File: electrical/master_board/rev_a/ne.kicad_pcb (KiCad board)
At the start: 2 copper layers, 0 parts

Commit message: Inject the PCB outlines into master/center/ne/nw/se/sw PCB's.
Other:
- board outline added: 42.2 x 39 mm
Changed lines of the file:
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@@
     (uvia_drill 0.1)
   )
+  (gr_line (start 162.50 64.00) (end 170.67 64.00) (layer Edge.Cuts) (width 0.05))
+  (gr_line (start 170.67 64.00) (end 170.80 63.99) (layer Edge.Cuts) (width 0.05))
+  (gr_line (start 170.80 63.99) (end 170.93 63.98) (layer Edge.Cuts) (width 0.05))
+  (gr_line (start 170.93 63.98) (end 171.06 63.95) (layer Edge.Cuts) (width 0.05))
+  (gr_line (start 171.06 63.95) (end 171.19 63.90) (layer Edge.Cuts) (width 0.05))
+  (gr_line (start 171.19 63.90) (end 171.32 63.85) (layer Edge.Cuts) (width 0.05))
+  (gr_line (start 171.32 63.85) (end 171.43 63.79) (layer Edge.Cuts) (width 0.05))
+  (gr_line (start 171.43 63.79) (end 171.55 63.72) (layer Edge.Cuts) (width 0.05))
+  (gr_line (start 171.55 63.72) (end 171.65 63.63) (layer Edge.Cuts) (width 0.05))
+  (gr_line (start 171.65 63.63) (end 171.75 63.54) (layer Edge.Cuts) (width 0.05))
+  (gr_line (start 171.75 63.54) (end 171.84 63.44) (layer Edge.Cuts) (width 0.05))
+  (gr_line (start 171.84 63.44) (end 171.92 63.33) (layer Edge.Cuts) (width 0.05))
+  (gr_line (start 171.92 63.33) (end 171.99 63.21) (layer Edge.Cuts) (width 0.05))
+  (gr_line (start 171.99 63.21) (end 172.04 63.09) (layer Edge.Cuts) (width 0.05))
+  (gr_line (start 172.04 63.09) (end 172.09 62.97) (layer Edge.Cuts) (width 0.05))
+  (gr_line (start 172.09 62.97) (end 172.13 62.84) (layer Edge.Cuts) (width 0.05))
+  (gr_line (start 172.13 62.84) (end 172.15 62.71) (layer Edge.Cuts) (width 0.05))
+  (gr_line (start 172.15 62.71) (end 172.16 62.57) (layer Edge.Cuts) (width 0.05))
+  (gr_line (start 172.16 62.57) (end 172.17 62.44) (layer Edge.Cuts) (width 0.05))
+  (gr_line (start 172.17 62.44) (end 172.15 62.31) (layer Edge.Cuts) (width 0.05))
+  (gr_line (start 172.15 62.31) (end 172.13 62.17) (layer Edge.Cuts) (width 0.05))
+  (gr_line (start 172.13 62.17) (end 172.10 62.04) (layer Edge.Cuts) (width 0.05))
+  (gr_line (start 172.10 62.04) (end 172.05 61.92) (layer Edge.Cuts) (width 0.05))
+  (gr_line (start 172.05 61.92) (end 171.99 61.80) (layer Edge.Cuts) (width 0.05))
+  (gr_line (start 171.99 61.80) (end 171.99 61.80) (layer Edge.Cuts) (width 0.05))
+  (gr_line (start 171.99 61.80) (end 167.96 55.01) (layer Edge.Cuts) (width 0.05))
+  (gr_line (start 167.96 55.01) (end 163.29 48.65) (layer Edge.Cuts) (width 0.05))
+  (gr_line (start 163.29 48.65) (end 158.02 42.77) (layer Edge.Cuts) (width 0.05))
+  (gr_line (start 158.02 42.77) (end 152.21 37.42) (layer Edge.Cuts) (width 0.05))
+  (gr_line (start 152.21 37.42) (end 145.92 32.67) (layer Edge.Cuts) (width 0.05))
+  (gr_line (start 145.92 32.67) (end 139.19 28.54) (layer Edge.Cuts) (width 0.05))
+  (gr_line (start 139.19 28.54) (end 132.09 25.08) (layer Edge.Cuts) (width 0.05))
+  (gr_line (start 132.09 25.08) (end 131.96 25.04) (layer Edge.Cuts) (width 0.05))
+  (gr_line (start 131.96 25.04) (end 131.83 25.00) (layer Edge.Cuts) (width 0.05))
+  (gr_line (start 131.83 25.00) (end 131.70 24.98) (layer Edge.Cuts) (width 0.05))
+  (gr_line (start 131.70 24.98) (end 131.57 24.96) (layer Edge.Cuts) (width 0.05))
+  (gr_line (start 131.57 24.96) (end 131.43 24.96) (layer Edge.Cuts) (width 0.05))
+  (gr_line (start 131.43 24.96) (end 131.30 24.98) (layer Edge.Cuts) (width 0.05))
+  (gr_line (start 131.30 24.98) (end 131.17 25.00) (layer Edge.Cuts) (width 0.05))
+  (gr_line (start 131.17 25.00) (end 131.04 25.04) (layer Edge.Cuts) (width 0.05))
+  (gr_line (start 131.04 25.04) (end 130.91 25.08) (layer Edge.Cuts) (width 0.05))
+  (gr_line (start 130.91 25.08) (end 130.79 25.14) (layer Edge.Cuts) (width 0.05))
+  (gr_line (start 130.79 25.14) (end 130.67 25.21) (layer Edge.Cuts) (width 0.05))
+  (gr_line (start 130.67 25.21) (end 130.57 25.29) (layer Edge.Cuts) (width 0.05))
+  (gr_line (start 130.57 25.29) (end 130.46 25.38) (layer Edge.Cuts) (width 0.05))
+  (gr_line (start 130.46 25.38) (end 130.37 25.48) (layer Edge.Cuts) (width 0.05))
+  (gr_line (start 130.37 25.48) (end 130.29 25.58) (layer Edge.Cuts) (width 0.05))
+  (gr_line (start 130.29 25.58) (end 130.21 25.69) (layer Edge.Cuts) (width 0.05))
+  (gr_line (start 130.21 25.69) (end 130.15 25.81) (layer Edge.Cuts) (width 0.05))
+  (gr_line (start 130.15 25.81) (end 130.10 25.94) (layer Edge.Cuts) (width 0.05))
+  (gr_line (start 130.10 25.94) (end 130.05 26.06) (layer Edge.Cuts) (width 0.05))
+  (gr_line (start 130.05 26.06) (end 130.02 26.19) (layer Edge.Cuts) (width 0.05))
+  (gr_line (start 130.02 26.19) (end 130.01 26.33) (layer Edge.Cuts) (width 0.05))
+  (gr_line (start 130.01 26.33) (end 130.00 26.46) (layer Edge.Cuts) (width 0.05))
+  (gr_line (start 130.00 26.46) (end 130.00 61.00) (layer Edge.Cuts) (width 0.05))
+  (gr_line (start 130.00 61.00) (end 161.00 61.00) (layer Edge.Cuts) (width 0.05))
+  (gr_line (start 161.00 61.00) (end 161.13 61.01) (layer Edge.Cuts) (width 0.05))
+  (gr_line (start 161.13 61.01) (end 161.26 61.02) (layer Edge.Cuts) (width 0.05))
+  (gr_line (start 161.26 61.02) (end 161.39 61.05) (layer Edge.Cuts) (width 0.05))
+  (gr_line (start 161.39 61.05) (end 161.51 61.09) (layer Edge.Cuts) (width 0.05))
+  (gr_line (start 161.51 61.09) (end 161.63 61.14) (layer Edge.Cuts) (width 0.05))
+  (gr_line (start 161.63 61.14) (end 161.75 61.20) (layer Edge.Cuts) (width 0.05))
+  (gr_line (start 161.75 61.20) (end 161.86 61.27) (layer Edge.Cuts) (width 0.05))
+  (gr_line (start 161.86 61.27) (end 161.96 61.35) (layer Edge.Cuts) (width 0.05))
+  (gr_line (start 161.96 61.35) (end 162.06 61.44) (layer Edge.Cuts) (width 0.05))
+  (gr_line (start 162.06 61.44) (end 162.15 61.54) (layer Edge.Cuts) (width 0.05))
+  (gr_line (start 162.15 61.54) (end 162.23 61.64) (layer Edge.Cuts) (width 0.05))
+  (gr_line (start 162.23 61.64) (end 162.30 61.75) (layer Edge.Cuts) (width 0.05))
+  (gr_line (start 162.30 61.75) (end 162.36 61.87) (layer Edge.Cuts) (width 0.05))
+  (gr_line (start 162.36 61.87) (end 162.41 61.99) (layer Edge.Cuts) (width 0.05))
+  (gr_line (start 162.41 61.99) (end 162.45 62.11) (layer Edge.Cuts) (width 0.05))
+  (gr_line (start 162.45 62.11) (end 162.48 62.24) (layer Edge.Cuts) (width 0.05))
+  (gr_line (start 162.48 62.24) (end 162.49 62.37) (layer Edge.Cuts) (width 0.05))
+  (gr_line (start 162.49 62.37) (end 162.50 62.50) (layer Edge.Cuts) (width 0.05))
+  (gr_line (start 162.50 62.50) (end 162.50 64.00) (layer Edge.Cuts) (width 0.05))
 )

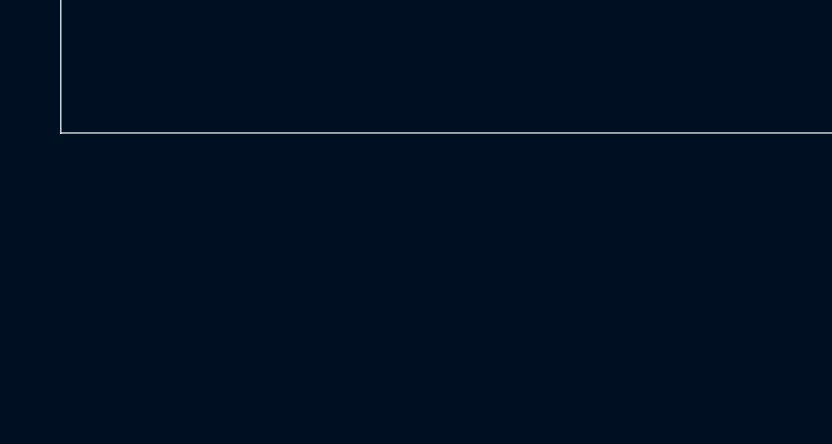
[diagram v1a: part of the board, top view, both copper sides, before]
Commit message: Have generated/footprint symbol in a KiCad project.
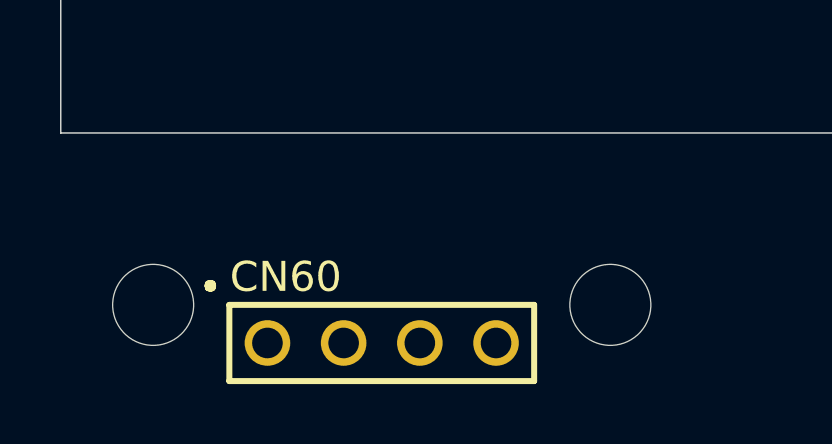
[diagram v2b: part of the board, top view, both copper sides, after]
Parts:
- added CN60: HCSR04H;F1X4, HR2:HCSR04_F1x4H_MATE, F.Cu at (140.7, 68.0)
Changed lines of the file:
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@@
   (general
     (thickness 1.6)
-    (drawings 0)
+    (drawings 75)
     (tracks 0)
     (zones 0)
-    (modules 0)
+    (modules 1)
     (nets 1)
   )
@@
     (47 F.CrtYd user)
     (48 B.Fab user)
-    (49 F.Fab user)
+    (49 F.Fab user hide)
   )
   (setup
@@
     (uvia_dia 0.3)
     (uvia_drill 0.1)
-  )
-  (gr_line (start 162.50 64.00) (end 170.67 64.00) (layer Edge.Cuts) (width 0.05))
-  (gr_line (start 170.67 64.00) (end 170.80 63.99) (layer Edge.Cuts) (width 0.05))
-  (gr_line (start 170.80 63.99) (end 170.93 63.98) (layer Edge.Cuts) (width 0.05))
+    (add_net "Net-(CN60-Pad1)")
+    (add_net "Net-(CN60-Pad2)")
+    (add_net "Net-(CN60-Pad3)")
+    (add_net "Net-(CN60-Pad4)")
+  )
+  (module HR2:HCSR04_F1x4H_MATE (layer F.Cu)
+    (at 140.7 68)
+    (fp_text reference CN60 (at -3.2 -2.2) (layer F.SilkS)
+      (effects (font (size 1 1) (thickness 0.2)))
+    )
+    (fp_text value HCSR04H;F1X4 (at 0 -2) (layer F.Fab)
+      (effects (font (size 1 1) (thickness 0.2)))
+    )
+    (fp_line (start 5.08 -1.27) (end 5.08 1.27) (layer F.SilkS) (width 0.2))
+    (fp_line (start 5.08 1.27) (end -5.08 1.27) (layer F.SilkS) (width 0.2))
+    (fp_line (start -5.08 1.27) (end -5.08 -1.27) (layer F.SilkS) (width 0.2))
+    (fp_line (start -5.08 -1.27) (end 5.08 -1.27) (layer F.SilkS) (width 0.2))
+    (fp_line (start -5.62 -1.91) (end -5.64 -1.98) (layer F.SilkS) (width 0.2))
+    (fp_line (start -5.64 -1.98) (end -5.71 -2) (layer F.SilkS) (width 0.2))
+    (fp_line (start -5.71 -2) (end -5.79 -1.98) (layer F.SilkS) (width 0.2))
+    (fp_line (start -5.79 -1.98) (end -5.81 -1.91) (layer F.SilkS) (width 0.2))
+    (fp_line (start -5.81 -1.91) (end -5.79 -1.83) (layer F.SilkS) (width 0.2))
+    (fp_line (start -5.79 -1.83) (end -5.71 -1.8) (layer F.SilkS) (width 0.2))
+    (fp_line (start -5.71 -1.8) (end -5.64 -1.83) (layer F.SilkS) (width 0.2))
+    (fp_line (start -5.64 -1.83) (end -5.62 -1.91) (layer F.SilkS) (width 0.2))
+    (pad "HCSR04 West Tie Down Hole" np_thru_hole circle (at -7.62 -1.27) (size 2.7 2.7) (drill 2.7) (layers *.Cu *.Mask))
+    (pad "HCSR04 East Tie Down Hole" np_thru_hole circle (at 7.62 -1.27) (size 2.7 2.7) (drill 2.7) (layers *.Cu *.Mask))
+    (pad 4 thru_hole circle (at 3.81 0) (size 1.52 1.52) (drill 1.02) (layers *.Cu *.Mask))
+    (pad 3 thru_hole circle (at 1.27 0) (size 1.52 1.52) (drill 1.02) (layers *.Cu *.Mask))
+    (pad 2 thru_hole circle (at -1.27 0) (size 1.52 1.52) (drill 1.02) (layers *.Cu *.Mask))
+    (pad 1 thru_hole circle (at -3.81 0) (size 1.52 1.52) (drill 1.02) (layers *.Cu *.Mask))
+  )
+  (gr_line (start 162.5 64) (end 170.67 64) (layer Edge.Cuts) (width 0.05))
+  (gr_line (start 170.67 64) (end 170.8 63.99) (layer Edge.Cuts) (width 0.05))
+  (gr_line (start 170.8 63.99) (end 170.93 63.98) (layer Edge.Cuts) (width 0.05))
   (gr_line (start 170.93 63.98) (end 171.06 63.95) (layer Edge.Cuts) (width 0.05))
-  (gr_line (start 171.06 63.95) (end 171.19 63.90) (layer Edge.Cuts) (width 0.05))
-  (gr_line (start 171.19 63.90) (end 171.32 63.85) (layer Edge.Cuts) (width 0.05))
+  (gr_line (start 171.06 63.95) (end 171.19 63.9) (layer Edge.Cuts) (width 0.05))
+  (gr_line (start 171.19 63.9) (end 171.32 63.85) (layer Edge.Cuts) (width 0.05))
   (gr_line (start 171.32 63.85) (end 171.43 63.79) (layer Edge.Cuts) (width 0.05))
   (gr_line (start 171.43 63.79) (end 171.55 63.72) (layer Edge.Cuts) (width 0.05))
@@
   (gr_line (start 172.17 62.44) (end 172.15 62.31) (layer Edge.Cuts) (width 0.05))
   (gr_line (start 172.15 62.31) (end 172.13 62.17) (layer Edge.Cuts) (width 0.05))
-  (gr_line (start 172.13 62.17) (end 172.10 62.04) (layer Edge.Cuts) (width 0.05))
-  (gr_line (start 172.10 62.04) (end 172.05 61.92) (layer Edge.Cuts) (width 0.05))
-  (gr_line (start 172.05 61.92) (end 171.99 61.80) (layer Edge.Cuts) (width 0.05))
-  (gr_line (start 171.99 61.80) (end 171.99 61.80) (layer Edge.Cuts) (width 0.05))
-  (gr_line (start 171.99 61.80) (end 167.96 55.01) (layer Edge.Cuts) (width 0.05))
+  (gr_line (start 172.13 62.17) (end 172.1 62.04) (layer Edge.Cuts) (width 0.05))
+  (gr_line (start 172.1 62.04) (end 172.05 61.92) (layer Edge.Cuts) (width 0.05))
+  (gr_line (start 172.05 61.92) (end 171.99 61.8) (layer Edge.Cuts) (width 0.05))
+  (gr_line (start 171.99 61.8) (end 171.99 61.8) (layer Edge.Cuts) (width 0.05))
+  (gr_line (start 171.99 61.8) (end 167.96 55.01) (layer Edge.Cuts) (width 0.05))
   (gr_line (start 167.96 55.01) (end 163.29 48.65) (layer Edge.Cuts) (width 0.05))
   (gr_line (start 163.29 48.65) (end 158.02 42.77) (layer Edge.Cuts) (width 0.05))
@@
   (gr_line (start 139.19 28.54) (end 132.09 25.08) (layer Edge.Cuts) (width 0.05))
   (gr_line (start 132.09 25.08) (end 131.96 25.04) (layer Edge.Cuts) (width 0.05))
-  (gr_line (start 131.96 25.04) (end 131.83 25.00) (layer Edge.Cuts) (width 0.05))
-  (gr_line (start 131.83 25.00) (end 131.70 24.98) (layer Edge.Cuts) (width 0.05))
-  (gr_line (start 131.70 24.98) (end 131.57 24.96) (layer Edge.Cuts) (width 0.05))
+  (gr_line (start 131.96 25.04) (end 131.83 25) (layer Edge.Cuts) (width 0.05))
+  (gr_line (start 131.83 25) (end 131.7 24.98) (layer Edge.Cuts) (width 0.05))
+  (gr_line (start 131.7 24.98) (end 131.57 24.96) (layer Edge.Cuts) (width 0.05))
   (gr_line (start 131.57 24.96) (end 131.43 24.96) (layer Edge.Cuts) (width 0.05))
-  (gr_line (start 131.43 24.96) (end 131.30 24.98) (layer Edge.Cuts) (width 0.05))
-  (gr_line (start 131.30 24.98) (end 131.17 25.00) (layer Edge.Cuts) (width 0.05))
-  (gr_line (start 131.17 25.00) (end 131.04 25.04) (layer Edge.Cuts) (width 0.05))
+  (gr_line (start 131.43 24.96) (end 131.3 24.98) (layer Edge.Cuts) (width 0.05))
+  (gr_line (start 131.3 24.98) (end 131.17 25) (layer Edge.Cuts) (width 0.05))
+  (gr_line (start 131.17 25) (end 131.04 25.04) (layer Edge.Cuts) (width 0.05))
   (gr_line (start 131.04 25.04) (end 130.91 25.08) (layer Edge.Cuts) (width 0.05))
   (gr_line (start 130.91 25.08) (end 130.79 25.14) (layer Edge.Cuts) (width 0.05))
@@
   (gr_line (start 130.29 25.58) (end 130.21 25.69) (layer Edge.Cuts) (width 0.05))
   (gr_line (start 130.21 25.69) (end 130.15 25.81) (layer Edge.Cuts) (width 0.05))
-  (gr_line (start 130.15 25.81) (end 130.10 25.94) (layer Edge.Cuts) (width 0.05))
-  (gr_line (start 130.10 25.94) (end 130.05 26.06) (layer Edge.Cuts) (width 0.05))
+  (gr_line (start 130.15 25.81) (end 130.1 25.94) (layer Edge.Cuts) (width 0.05))
+  (gr_line (start 130.1 25.94) (end 130.05 26.06) (layer Edge.Cuts) (width 0.05))
   (gr_line (start 130.05 26.06) (end 130.02 26.19) (layer Edge.Cuts) (width 0.05))
   (gr_line (start 130.02 26.19) (end 130.01 26.33) (layer Edge.Cuts) (width 0.05))
-  (gr_line (start 130.01 26.33) (end 130.00 26.46) (layer Edge.Cuts) (width 0.05))
-  (gr_line (start 130.00 26.46) (end 130.00 61.00) (layer Edge.Cuts) (width 0.05))
-  (gr_line (start 130.00 61.00) (end 161.00 61.00) (layer Edge.Cuts) (width 0.05))
-  (gr_line (start 161.00 61.00) (end 161.13 61.01) (layer Edge.Cuts) (width 0.05))
+  (gr_line (start 130.01 26.33) (end 130 26.46) (layer Edge.Cuts) (width 0.05))
+  (gr_line (start 130 26.46) (end 130 61) (layer Edge.Cuts) (width 0.05))
+  (gr_line (start 130 61) (end 161 61) (layer Edge.Cuts) (width 0.05))
+  (gr_line (start 161 61) (end 161.13 61.01) (layer Edge.Cuts) (width 0.05))
   (gr_line (start 161.13 61.01) (end 161.26 61.02) (layer Edge.Cuts) (width 0.05))
   (gr_line (start 161.26 61.02) (end 161.39 61.05) (layer Edge.Cuts) (width 0.05))
   (gr_line (start 161.39 61.05) (end 161.51 61.09) (layer Edge.Cuts) (width 0.05))
   (gr_line (start 161.51 61.09) (end 161.63 61.14) (layer Edge.Cuts) (width 0.05))
-  (gr_line (start 161.63 61.14) (end 161.75 61.20) (layer Edge.Cuts) (width 0.05))
-  (gr_line (start 161.75 61.20) (end 161.86 61.27) (layer Edge.Cuts) (width 0.05))
+  (gr_line (start 161.63 61.14) (end 161.75 61.2) (layer Edge.Cuts) (width 0.05))
+  (gr_line (start 161.75 61.2) (end 161.86 61.27) (layer Edge.Cuts) (width 0.05))
   (gr_line (start 161.86 61.27) (end 161.96 61.35) (layer Edge.Cuts) (width 0.05))
   (gr_line (start 161.96 61.35) (end 162.06 61.44) (layer Edge.Cuts) (width 0.05))
   (gr_line (start 162.06 61.44) (end 162.15 61.54) (layer Edge.Cuts) (width 0.05))
   (gr_line (start 162.15 61.54) (end 162.23 61.64) (layer Edge.Cuts) (width 0.05))
-  (gr_line (start 162.23 61.64) (end 162.30 61.75) (layer Edge.Cuts) (width 0.05))
-  (gr_line (start 162.30 61.75) (end 162.36 61.87) (layer Edge.Cuts) (width 0.05))
+  (gr_line (start 162.23 61.64) (end 162.3 61.75) (layer Edge.Cuts) (width 0.05))
+  (gr_line (start 162.3 61.75) (end 162.36 61.87) (layer Edge.Cuts) (width 0.05))
   (gr_line (start 162.36 61.87) (end 162.41 61.99) (layer Edge.Cuts) (width 0.05))
   (gr_line (start 162.41 61.99) (end 162.45 62.11) (layer Edge.Cuts) (width 0.05))
   (gr_line (start 162.45 62.11) (end 162.48 62.24) (layer Edge.Cuts) (width 0.05))
   (gr_line (start 162.48 62.24) (end 162.49 62.37) (layer Edge.Cuts) (width 0.05))
-  (gr_line (start 162.49 62.37) (end 162.50 62.50) (layer Edge.Cuts) (width 0.05))
-  (gr_line (start 162.50 62.50) (end 162.50 64.00) (layer Edge.Cuts) (width 0.05))
+  (gr_line (start 162.49 62.37) (end 162.5 62.5) (layer Edge.Cuts) (width 0.05))
+  (gr_line (start 162.5 62.5) (end 162.5 64) (layer Edge.Cuts) (width 0.05))
 )

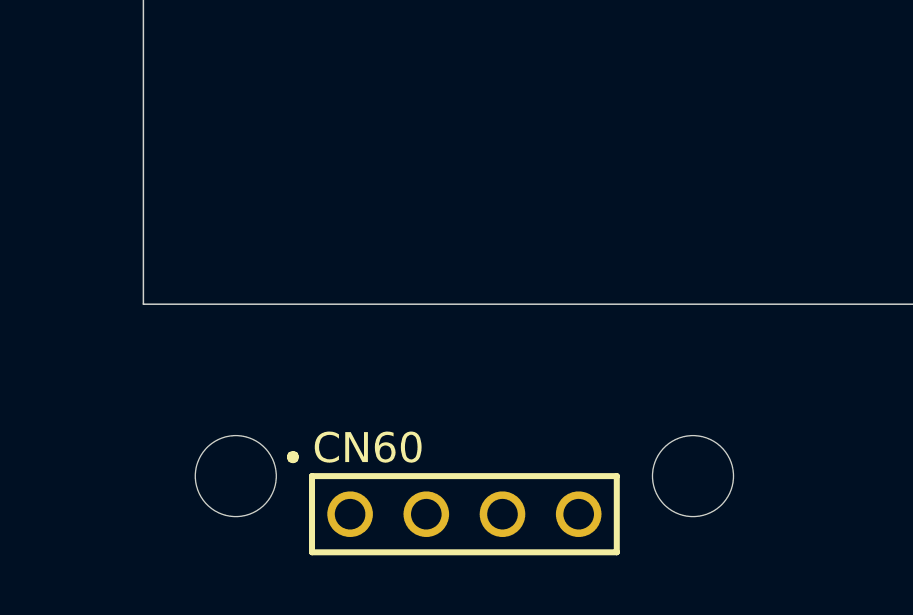
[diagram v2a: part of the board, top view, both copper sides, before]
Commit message: Updated some of the schematics and PCB's via hr2_models.py .
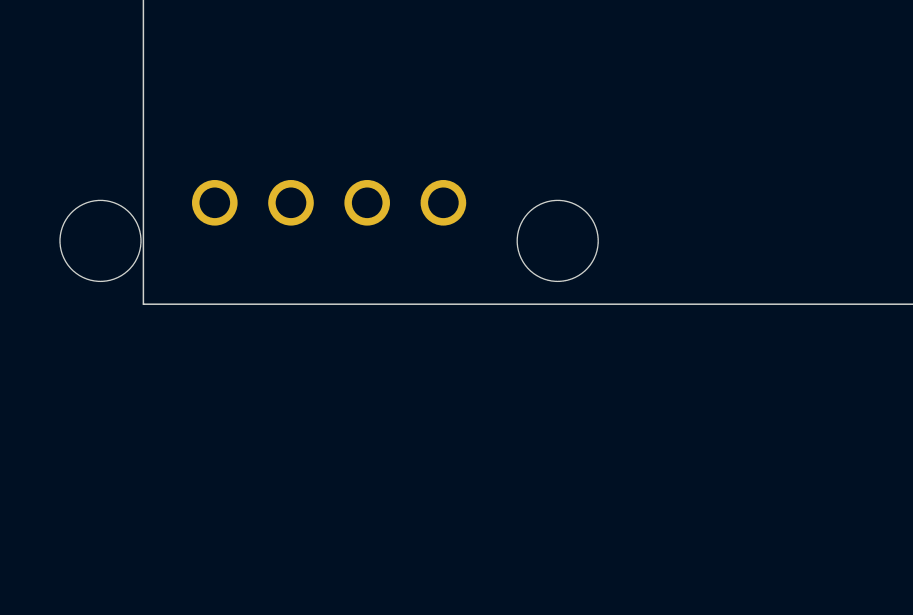
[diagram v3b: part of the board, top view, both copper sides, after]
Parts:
- CN60: moved to B.Cu
- moved CN60 11.3 mm to (136.2, 57.6)
